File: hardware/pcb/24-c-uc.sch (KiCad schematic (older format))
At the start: 29 parts, among them J201 ST-LINK, J202 Debug UART, U201 STM32F103C8Tx, Y201 8MHz

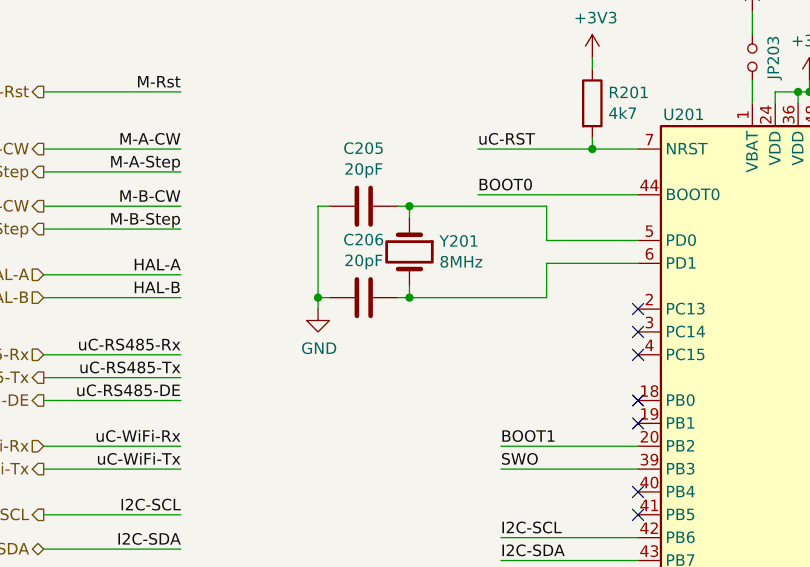
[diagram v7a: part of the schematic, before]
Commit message: changed crystals
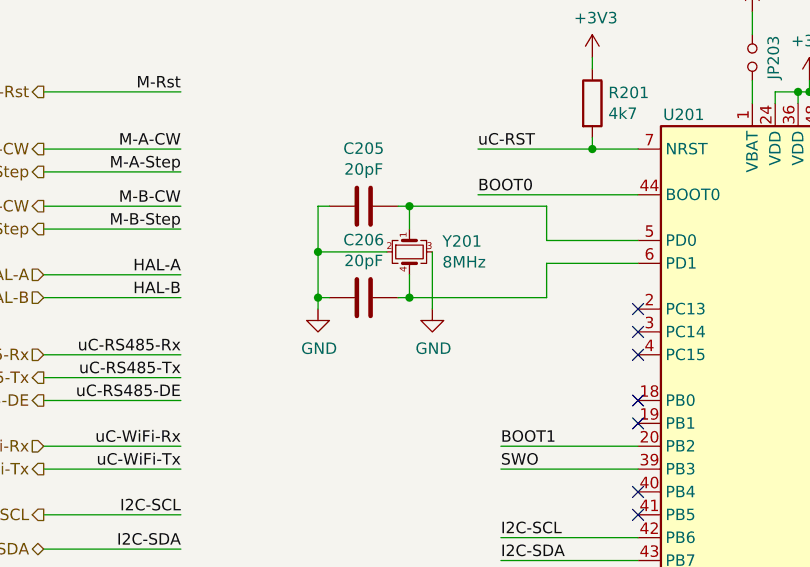
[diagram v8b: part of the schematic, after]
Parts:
- removed Y201: 8MHz, symbol Device:Crystal
- added Y201: 8MHz, Crystal:Crystal_SMD_5032-4Pin_5.0x3.2mm, symbol Device:Crystal_GND23_Small
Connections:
- net GND: now also Y201.2, Y201.3
- net at C205.1, U201.5 (PD0): now also Y201.1
- net at C206.1, U201.6 (PD1): now also Y201.4
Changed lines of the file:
@@
-$EndComp
-$Comp
-L Device:Crystal Y201
-U 1 1 5FE61E24
-P 4000 2350
-F 0 "Y201" V 3954 2481 50  0000 L CNN
-F 1 "8MHz" V 4045 2481 50  0000 L CNN
-F 2 "" H 4000 2350 50  0001 C CNN
-F 3 "~" H 4000 2350 50  0001 C CNN
-	1    4000 2350
-	0    1    1    0
 $EndComp
 $Comp
@@
 	3650 2150 3600 2150
 Wire Wire Line
-	3600 2150 3600 2550
+	3600 2150 3600 2350
 Wire Wire Line
 	3600 2550 3650 2550
@@
 Wire Wire Line
 	4600 2150 4000 2150
-Wire Wire Line
-	4000 2200 4000 2150
 Connection ~ 4000 2150
 Wire Wire Line
 	4000 2150 3950 2150
-Wire Wire Line
-	4000 2500 4000 2550
 Connection ~ 4000 2550
 Wire Wire Line
@@
 Wire Wire Line
 	1400 6600 2100 6600
+$Comp
+L Device:Crystal_GND23_Small Y201
+U 1 1 5FE749A7
+P 4000 2350
+F 0 "Y201" V 3954 2494 50  0000 L CNN
+F 1 "8MHz" V 4045 2494 50  0000 L CNN
+F 2 "Crystal:Crystal_SMD_5032-4Pin_5.0x3.2mm" H 4000 2350 50  0001 C CNN
+F 3 "~" H 4000 2350 50  0001 C CNN
+	1    4000 2350
+	0    1    1    0
+$EndComp
+Wire Wire Line
+	4000 2150 4000 2250
+Wire Wire Line
+	4000 2450 4000 2550
+Wire Wire Line
+	3900 2350 3600 2350
+Connection ~ 3600 2350
+Wire Wire Line
+	3600 2350 3600 2550
+$Comp
+L power:GND #PWR?
+U 1 1 5FE85E24
+P 4100 2600
+AR Path="/5FE85E24" Ref="#PWR?"  Part="1"
+AR Path="/5FDEAABE/5FE85E24" Ref="#PWR?"  Part="1"
+F 0 "#PWR?" H 4100 2350 50  0001 C CNN
+F 1 "GND" H 4105 2427 50  0000 C CNN
+F 2 "" H 4100 2600 50  0001 C CNN
+F 3 "" H 4100 2600 50  0001 C CNN
+	1    4100 2600
+	1    0    0    -1
+$EndComp
+Wire Wire Line
+	4100 2600 4100 2350
 $EndSCHEMATC
